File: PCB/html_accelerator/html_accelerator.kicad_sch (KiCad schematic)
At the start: 12 parts, among them J2 Bus_PCI_Express_x8, J3 PCIexpress_bracket, U10 MX30LF1G28AD-TI, U2 AU6438BS, U3 MX30LF1G28AD-TI, U4 AU6438BS, U5 AU6438BS, U7 AU6438BS, U8 MX30LF1G28AD-TI, U9 MX30LF1G28AD-TI

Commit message: Sch Symbol updates and cleanup
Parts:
- added unit 4 of U1
- added unit 5 of U1
- added unit 2 of U1
- added unit 3 of U1
- added U11, U12, U13: ~, Package_QFP:LQFP-128_14x20mm_P0.5mm, symbol html_accel_Symbols:VT6212
- added unit 5 of U6
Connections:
- net at U3.29 (I/O0): no longer U8.16 (CLE)
- net at U3.30 (I/O1): no longer U8.38 (PT)
- net at U3.32 (I/O3): no longer U8.8 (RE#)
- net at U3.42 (I/O5): no longer U8.18 (WE#)
- net at U3.43 (I/O6): no longer U8.19 (WP#)
- net at U3.7 (STATUS): no longer U8.17 (ALE)
- net at U9.29 (I/O0): no longer U10.16 (CLE)
- net at U9.30 (I/O1): no longer U10.38 (PT)
- net at U9.32 (I/O3): no longer U10.8 (RE#)
- net at U9.42 (I/O5): no longer U10.18 (WE#)
- net at U9.43 (I/O6): no longer U10.19 (WP#)
- net at U9.7 (STATUS): no longer U10.17 (ALE)
- new net: U1.103 (NC), U1.20 (#FRAME)
- new net: U1.104 (NC), U1.24 (#STOP)
- new net: U1.58 (NC), U1.6 (IDSEL)
- new net: U1.23 (#DEV_SEL), U1.97 (NC)
- new net: U1.60 (#SMI), U1.85 (USB_1N)
- new net: U11.60 (#SMI), U12.85 (USB_1N)

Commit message: update symbols and create sch pages
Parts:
- removed J2: Bus_PCI_Express_x8, Connector_PCBEdge:BUS_PCIexpress_x8, symbol Connector:Bus_PCI_Express_x8
- removed J3: PCIexpress_bracket, html_accel_footprints:PCIexpress_bracket_full, symbol html_accel_Symbols:PCIexpress_bracket
- removed U1, U11, U12, U13, U6: ~, Package_QFP:LQFP-128_14x20mm_P0.5mm, symbol html_accel_Symbols:VT6212
- removed U2: AU6438BS, Package_SO:SSOP-28_3.9x9.9mm_P0.635mm, symbol html_accel_Symbols:AU6438BS
- removed U3: MX30LF1G28AD-TI, html_accel_footprints:MX30LF1G28AD-TI, symbol html_accel_Symbols:MX30LF1G28AD-TI
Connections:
- net at U9.22 (NC): now also U10.1 (NC)
- net at U9.23 (NC): now also U10.2 (NC)
- net at U9.24 (NC): now also U10.3 (NC)
- net at U9.26 (NC): now also U10.4 (NC)
- net at U9.27 (NC): now also U10.5 (NC)
- net at U9.28 (NC): now also U10.6 (NC)
- net at U9.33 (NC): now also U10.10 (NC)
- net at U9.35 (NC): now also U10.11 (NC)
- net at U9.40 (NC): now also U10.14 (NC)
- net at U9.45 (NC): now also U10.15 (NC)
- net at U9.46 (NC): now also U10.20 (NC)
- net at U9.47 (NC): now also U10.21 (NC)
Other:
- added sheet FLASH_CTRL (3_FLASH_CTRL.kicad_sch)
- added sheet PCIE_Slot (2_PCI_SLOT.kicad_sch)
- moved on the sheet: U10A, U10B, U4, U5, U7, U8A, U8B, U9A, U9B

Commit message: Schematic edits
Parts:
- removed U10, U8, U9: MX30LF1G28AD-TI, html_accel_footprints:MX30LF1G28AD-TI, symbol html_accel_Symbols:MX30LF1G28AD-TI
- removed U4, U5, U7: AU6438BS, Package_SO:SSOP-28_3.9x9.9mm_P0.635mm, symbol html_accel_Symbols:AU6438BS
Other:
- added sheet PCIE_GPIO (PCIE_GPIO.kicad_sch)
- added sheet PCIE_POWER (PCIE_POWER.kicad_sch)
- added sheet PCIE_USB (PCIE_USB.kicad_sch)
- sheet FLASH_CTRL: file 3_FLASH_CTRL.kicad_sch -> FLASH_CTRL.kicad_sch
- sheet PCIE_Slot: file 2_PCI_SLOT.kicad_sch -> PCI_SLOT.kicad_sch

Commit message: schematic updates
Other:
- sheet FLASH_CTRL renamed eMMC1
- sheet PCIE_GPIO renamed PCIE_CONFIG_GPIO
- sheet eMMC1: file FLASH_CTRL.kicad_sch -> eMMC1.kicad_sch
- title: (none) -> HTML Accelerator
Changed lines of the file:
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@@
 (kicad_sch (version 20230121) (generator eeschema)
   (paper "A4")
+  (title_block
+    (title "HTML Accelerator")
+    (date "2024-09-15")
+    (rev "1")
+  )
   (sheet (at 25.4 25.4) (size 36.83 20.32) (fields_autoplaced)
     (stroke (width 0.1524) (type solid))
@@
     (stroke (width 0.1524) (type solid))
     (fill (color 0 0 0 0.0000))
-    (property "Sheetname" "FLASH_CTRL" (at 83.82 24.6884 0)
+    (property "Sheetname" "eMMC1" (at 83.82 24.6884 0)
       (effects (font (size 1.27 1.27)) (justify left bottom))
     )
-    (property "Sheetfile" "FLASH_CTRL.kicad_sch" (at 83.82 46.3046 0)
+    (property "Sheetfile" "eMMC1.kicad_sch" (at 83.82 46.3046 0)
       (effects (font (size 1.27 1.27)) (justify left top))
     )
@@
     (stroke (width 0.1524) (type solid))
     (fill (color 0 0 0 0.0000))
-    (property "Sheetname" "PCIE_GPIO" (at 25.4 107.2384 0)
+    (property "Sheetname" "PCIE_CONFIG_GPIO" (at 25.4 107.2384 0)
       (effects (font (size 1.27 1.27)) (justify left bottom))
     )

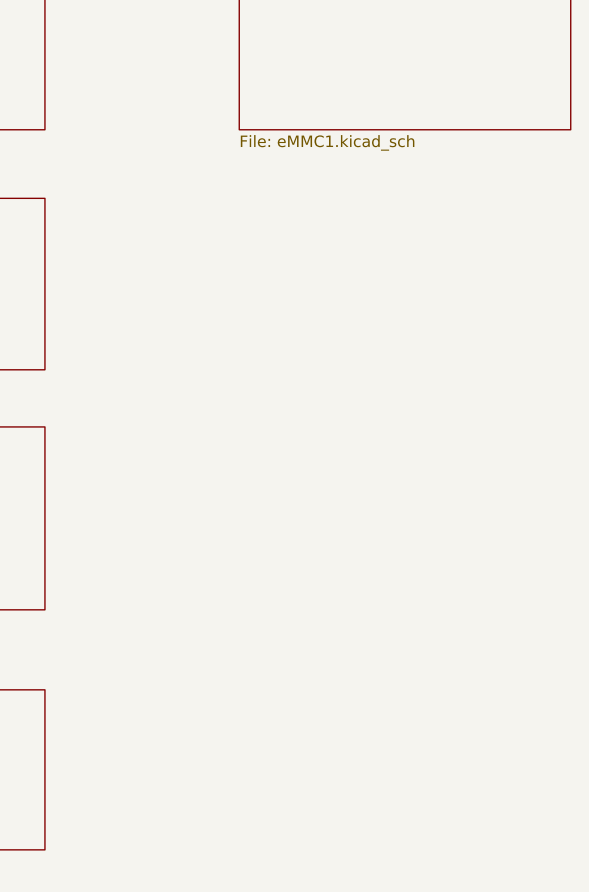
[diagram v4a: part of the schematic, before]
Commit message: EMMC symbols and netlist
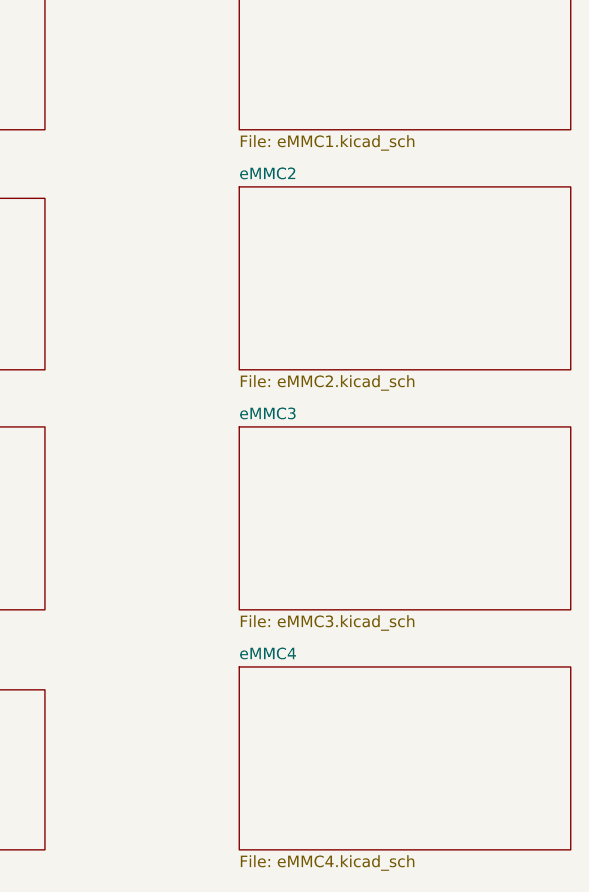
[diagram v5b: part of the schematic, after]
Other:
- added sheet eMMC2 (eMMC2.kicad_sch)
- added sheet eMMC3 (eMMC3.kicad_sch)
- added sheet eMMC4 (eMMC4.kicad_sch)
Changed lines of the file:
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@@
+    )
+  )
+  (sheet (at 83.82 52.07) (size 36.83 20.32) (fields_autoplaced)
+    (stroke (width 0.1524) (type solid))
+    (fill (color 0 0 0 0.0000))
+    (property "Sheetname" "eMMC2" (at 83.82 51.3584 0)
+      (effects (font (size 1.27 1.27)) (justify left bottom))
+    )
+    (property "Sheetfile" "eMMC2.kicad_sch" (at 83.82 72.9746 0)
+      (effects (font (size 1.27 1.27)) (justify left top))
+    )
+    (instances
+      (project "html_accelerator"
+        (path "/12b3a7c9-141f-40ba-9ebb-094b58bfa6c7" (page "12"))
+      )
     )
   )
@@
     (instances
       (project "html_accelerator"
-        (path "/12b3a7c9-141f-40ba-9ebb-094b58bfa6c7" (page "10"))
+        (path "/12b3a7c9-141f-40ba-9ebb-094b58bfa6c7" (page "11"))
+      )
+    )
+  )
+  (sheet (at 83.82 78.74) (size 36.83 20.32) (fields_autoplaced)
+    (stroke (width 0.1524) (type solid))
+    (fill (color 0 0 0 0.0000))
+    (property "Sheetname" "eMMC3" (at 83.82 78.0284 0)
+      (effects (font (size 1.27 1.27)) (justify left bottom))
+    )
+    (property "Sheetfile" "eMMC3.kicad_sch" (at 83.82 99.6446 0)
+      (effects (font (size 1.27 1.27)) (justify left top))
+    )
+    (instances
+      (project "html_accelerator"
+        (path "/12b3a7c9-141f-40ba-9ebb-094b58bfa6c7" (page "13"))
       )
     )
@@
     )
   )
+  (sheet (at 83.82 105.41) (size 36.83 20.32) (fields_autoplaced)
+    (stroke (width 0.1524) (type solid))
+    (fill (color 0 0 0 0.0000))
+    (property "Sheetname" "eMMC4" (at 83.82 104.6984 0)
+      (effects (font (size 1.27 1.27)) (justify left bottom))
+    )
+    (property "Sheetfile" "eMMC4.kicad_sch" (at 83.82 126.3146 0)
+      (effects (font (size 1.27 1.27)) (justify left top))
+    )
+    (instances
+      (project "html_accelerator"
+        (path "/12b3a7c9-141f-40ba-9ebb-094b58bfa6c7" (page "14"))
+      )
+    )
+  )
   (sheet_instances
-    (path "/" (page "1"))
+    (path "/" (page "13"))
   )
 )

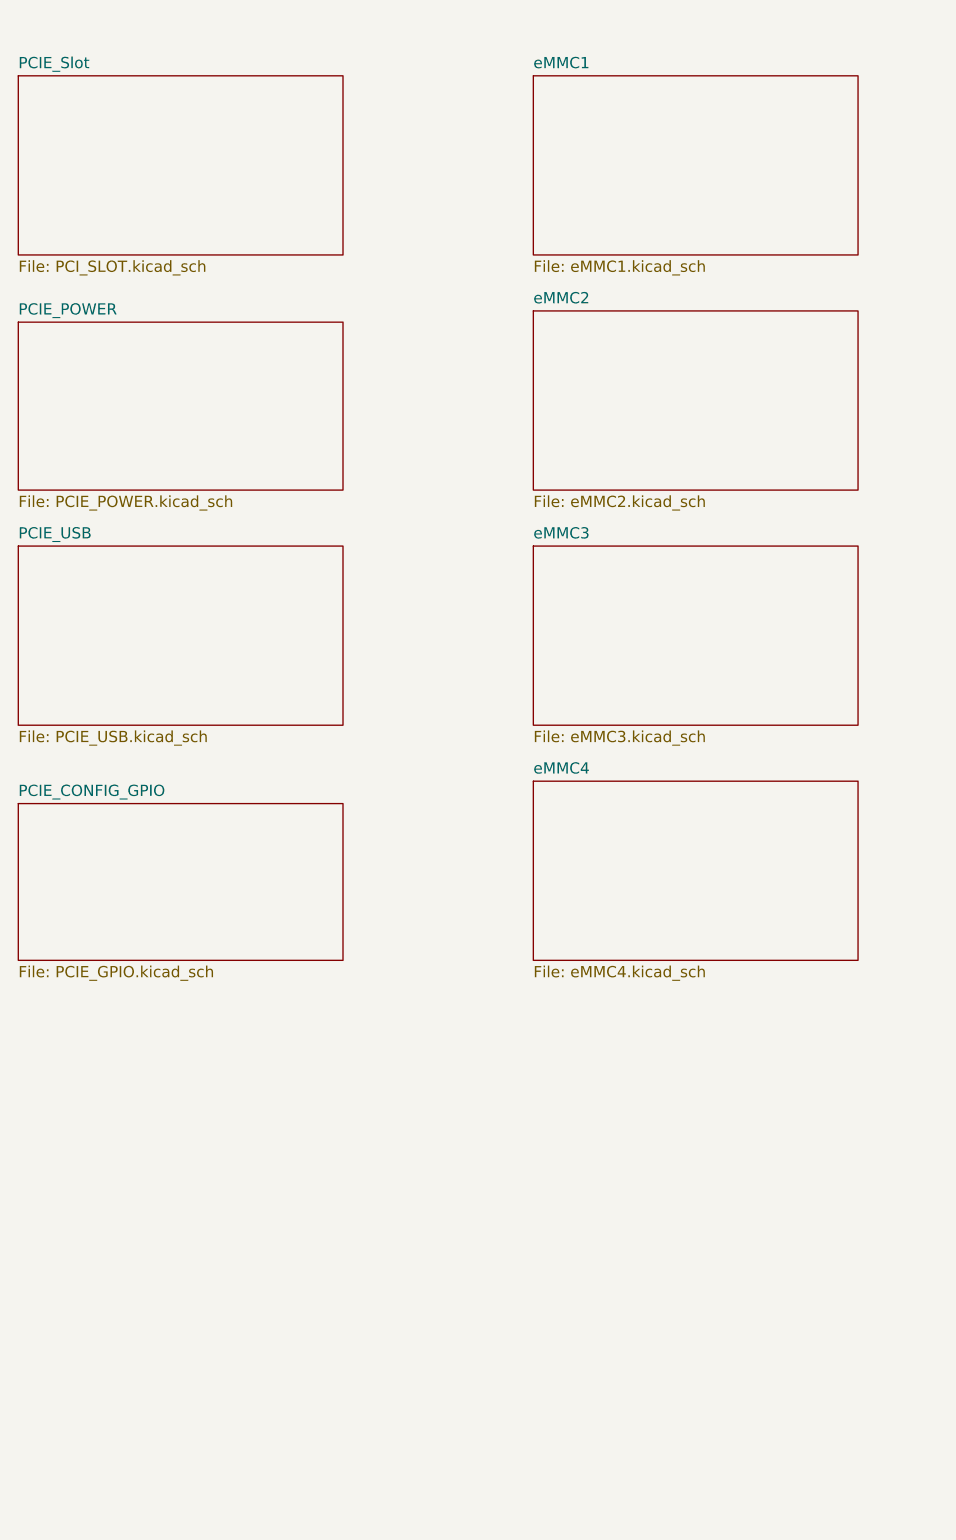
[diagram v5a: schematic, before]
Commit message: provision for LEDs
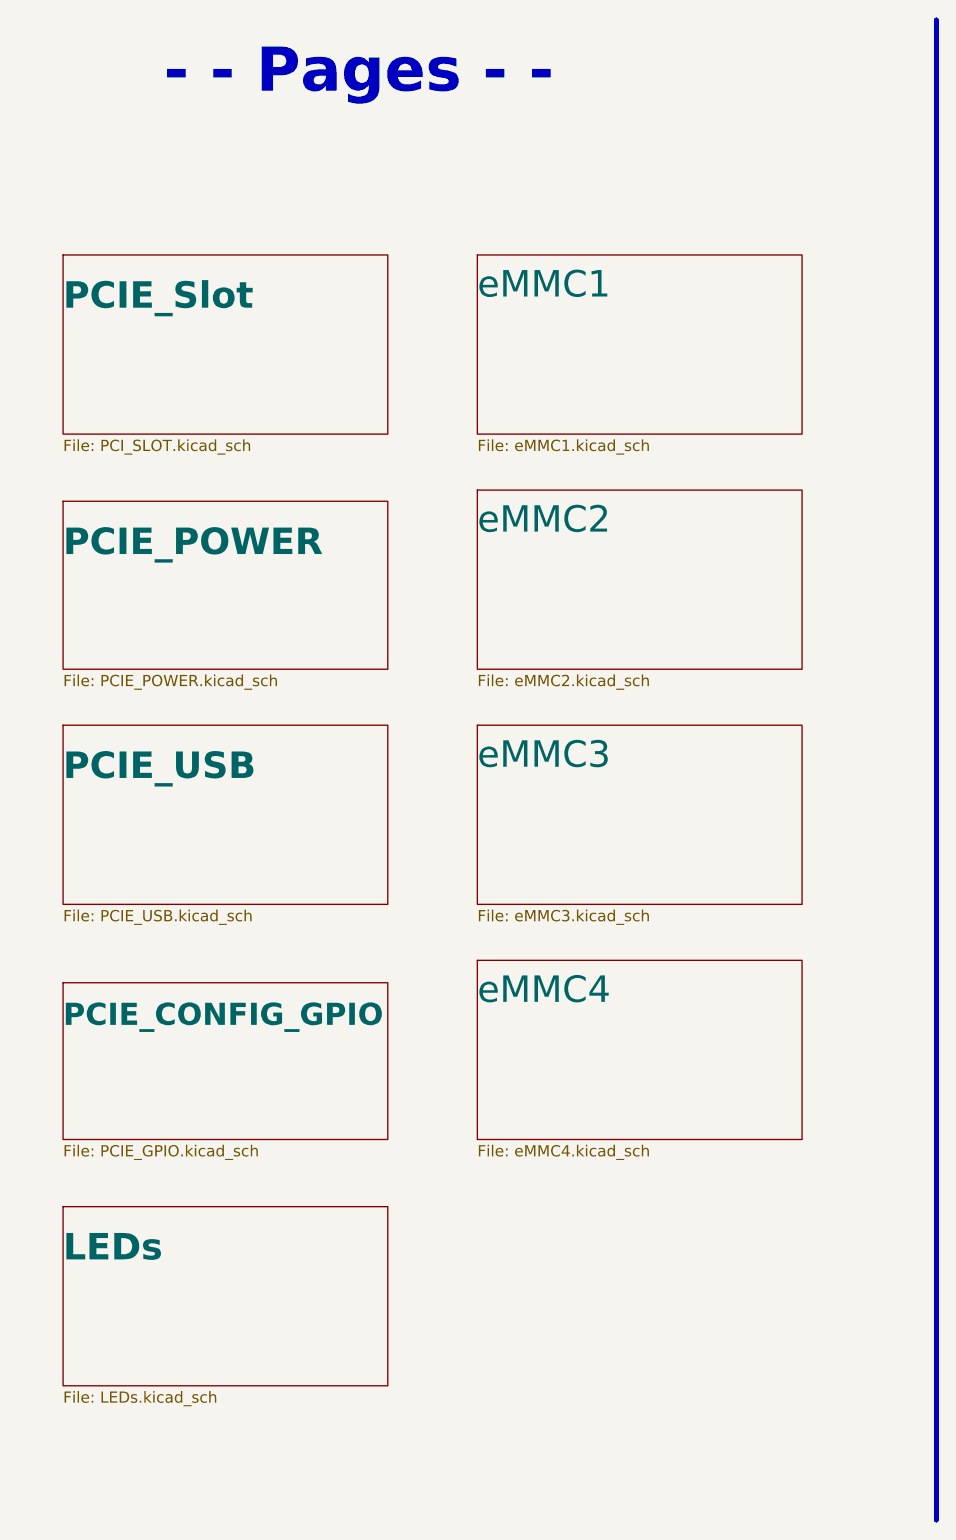
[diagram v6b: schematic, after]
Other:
- added sheet LEDs (LEDs.kicad_sch)
- note added: "- - Pages - -"

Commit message: placement updates
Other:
- added sheet Greebles (greebles.kicad_sch)
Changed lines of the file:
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@@
     (fill (type none))
   )
-  (image (at 207.01 91.44) (scale 0.466458)
+  (image (at 207.01 91.44) (scale 0.990302)
     (data
       iVBORw0KGgoAAAANSUhEUgAABkUAAAYJCAIAAABgEIkQAAAAA3NCSVQICAjb4U/gAAAACXBIWXMA
-      ABYlAAAWJQFJUiTwAAAgAElEQVR4nOzdebxkZ1Xo/d96nmfvqnNOd2dmEgNICFMwQIIyDzIpcgWE
+      ABXgAAAV4AGNVCw4AAAgAElEQVR4nOzdebxkZ1Xo/d96nmfvqnNOd2dmEgNICFMwQIIyDzIpcgWE
       QBRBQNBXBa5XuK8T3sEritcB4XIFARGJyEwgEKZIJmSQMIYAAkkIQ+ah093nnKq9n2HdP55ddep0
       dyJBI33S6/vp5AxVtWsPz66qvc5a6xFVxRhjjDHGGGOMMcaYLcL9oFfAGGOMMcYYY4wxxpibwOJZ
@@
       )
     )
+  )
+  (sheet (at 77.47 153.67) (size 36.83 20.32)
+    (stroke (width 0.1524) (type solid))
+    (fill (color 0 0 0 0.0000))
+    (property "Sheetname" "Greebles" (at 77.47 160.02 0)
+      (effects (font (size 3 3) bold) (justify left bottom))
+    )
+    (property "Sheetfile" "greebles.kicad_sch" (at 77.47 174.5746 0)
+      (effects (font (size 1.27 1.27)) (justify left top))
+    )
+    (instances
+      (project "html_accelerator"
+        (path "/12b3a7c9-141f-40ba-9ebb-094b58bfa6c7" (page "7"))
+      )
+    )
